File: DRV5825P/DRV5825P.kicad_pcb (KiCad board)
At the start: 2 copper layers, 65 x 70 mm, 43 parts, among them J1 Power_in, J2 Data_I/O, J3 CH_A, J4 CH_B, U1 DRV5825P

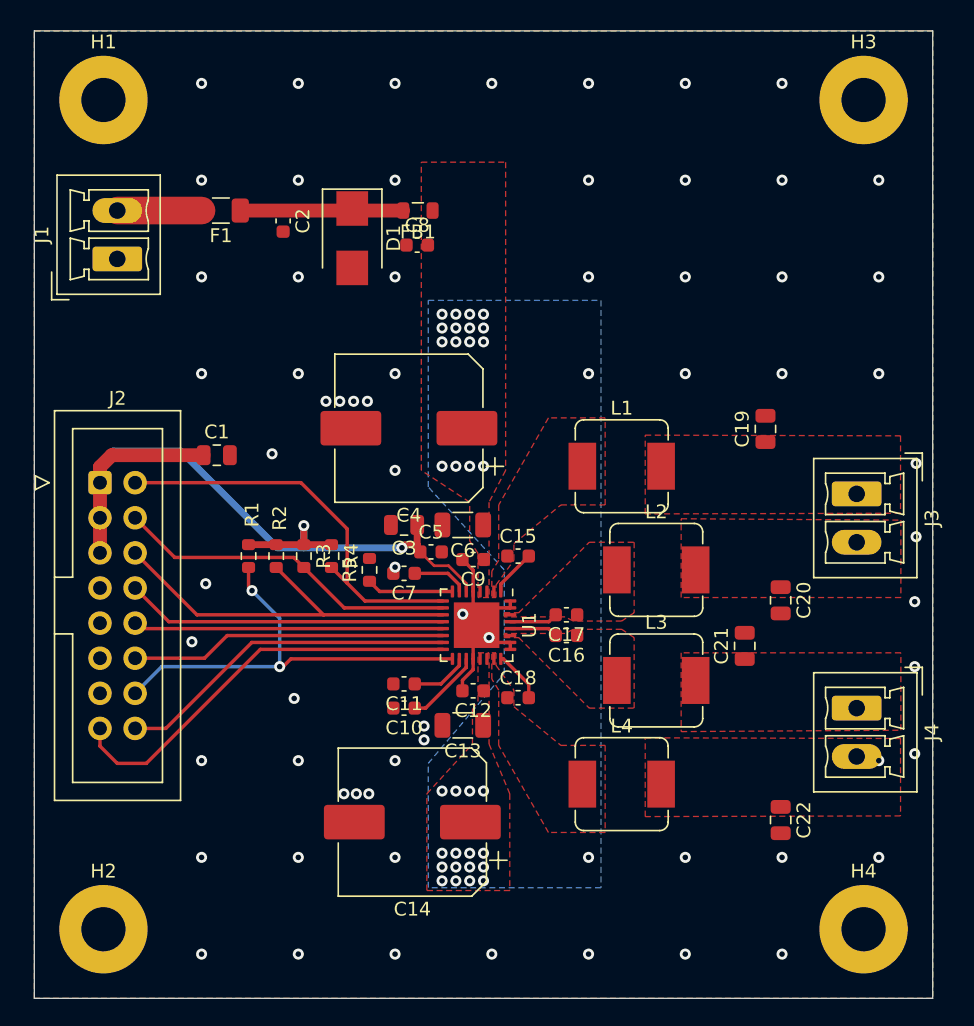
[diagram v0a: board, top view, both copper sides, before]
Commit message: teardrops added
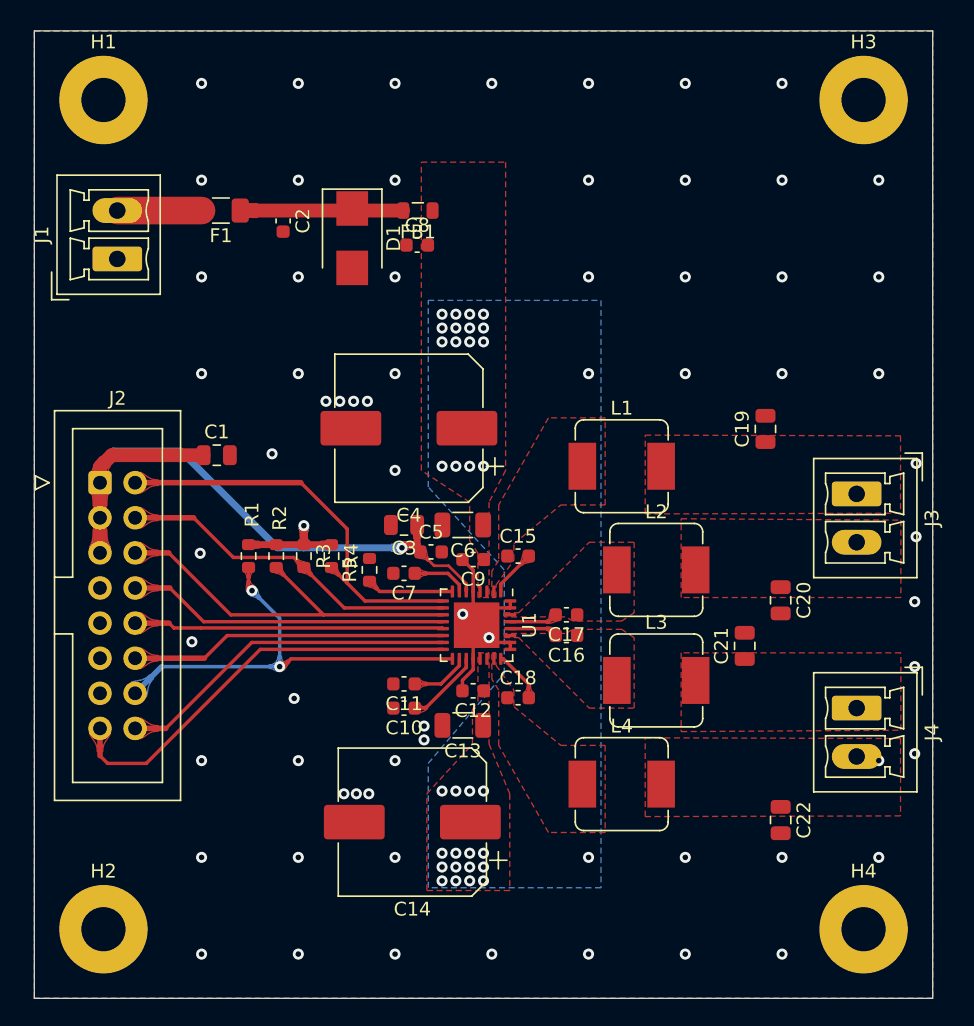
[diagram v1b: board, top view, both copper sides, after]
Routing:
- net GND: vias 67 -> 66

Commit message: gerbers ready
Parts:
- renumbered J2 to Data_CTL_I/O, J3 to OUT_A, J4 to OUT_B, J1 to Pwr_IN
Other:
- board text added: "+"
- board text added: "-"
- board text added: "GPIO0"
- board text added: "GPIO1"
- board text added: "GPIO2"
- board text added: "LRCLK"
- board text added: "SCL"
- board text added: "SCLK"
- board text added: "SDA"
- board text added: "SDIN"
- board text added: "~PDN"
